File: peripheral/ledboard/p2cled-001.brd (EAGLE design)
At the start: 91 x 55 mm, 5 parts, among them J3 DISP, J4 PWR

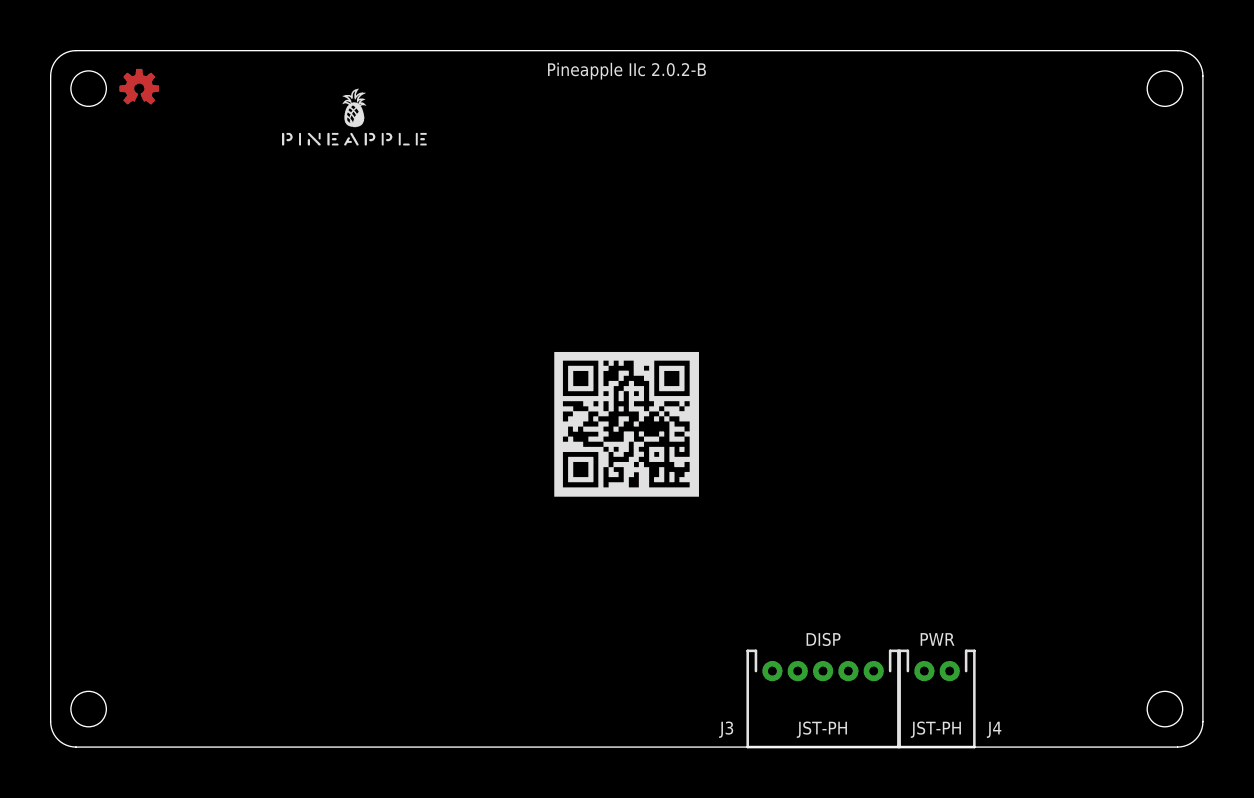
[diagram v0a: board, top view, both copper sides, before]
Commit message: Added LED board design.
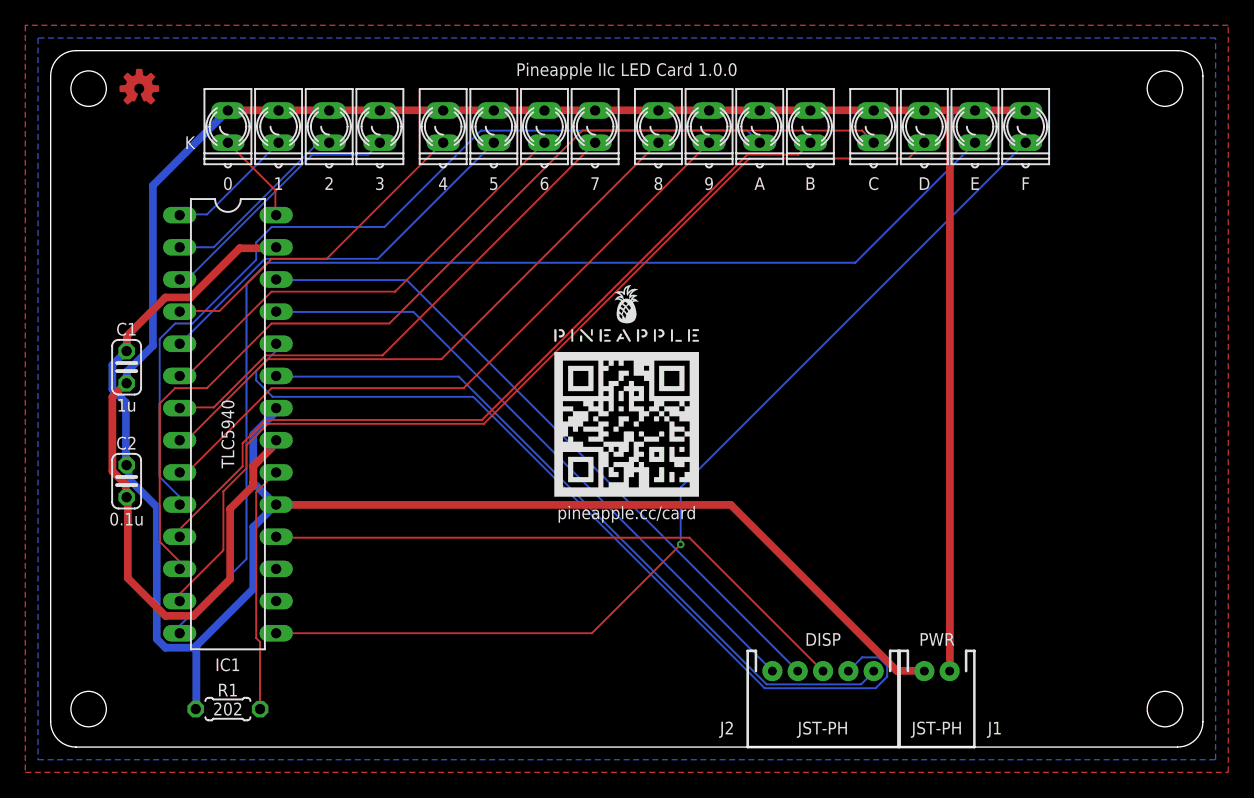
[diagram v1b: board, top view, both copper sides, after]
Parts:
- added 0, 1, 2, 3, 4, 5, 6, 7, 8, 9, A, B, C, D, E, F: (no value), led:Q62902-B152
- added C1: 1u, resistor:C025-024X044
- added C2: 0.1u, resistor:C025-024X044
- added IC1: TLC5940NT, tlc5940:DIL28-3
- added R1: 2k, resistor:0204/5
- moved U$1 26.5 mm to (45.5, 32.0)
- renumbered J3 to J2, J4 to J1
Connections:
- new net D5: IC1.23, J2.1
- new net D7: IC1.24, J2.2
- new net D8: IC1.18, J2.3
- new net MOSI: IC1.26, J2.4
- new net N$1: 0.K, IC1.28
- new net N$10: 9.K, IC1.9
- new net N$11: A.K, IC1.10
- new net N$12: B.K, IC1.11
- new net N$13: C.K, IC1.12
- new net N$14: D.K, IC1.13
- new net N$15: E.K, IC1.14
- new net N$16: F.K, IC1.15
- new net N$17: IC1.20, R1.2
- new net N$2: 1.K, IC1.1
- new net N$3: 2.K, IC1.2
- new net N$4: 3.K, IC1.3
- new net N$5: 4.K, IC1.4
- new net N$6: 5.K, IC1.5
- new net N$7: 6.K, IC1.6
- new net N$8: 7.K, IC1.7
- new net N$9: 8.K, IC1.8
- new net SCLK: IC1.25, J2.5
- net GND: now also C1.2, C2.2, IC1.19, IC1.22, IC1.27, R1.1
- net VCC: now also 0.A, 1.A, 2.A, 3.A, 4.A, 5.A, 6.A, 7.A, 8.A, 9.A, A.A, B.A, C.A, C1.1, C2.1, D.A, E.A, F.A, IC1.21
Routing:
- net VCC: track 0.00 -> 171.7 mm
- net GND: track 0.00 -> 128.5 mm
- net N$15: track 0.00 -> 92.0 mm
- net N$13: track 0.00 -> 79.5 mm
- net N$14: track 0.00 -> 77.9 mm
- net N$16: track 0.00 -> 77.9 mm, vias 0 -> 1
- net N$11: track 0.00 -> 69.1 mm
- net D7: track 0.00 -> 68.5 mm
- net N$12: track 0.00 -> 64.1 mm
- net D5: track 0.00 -> 57.8 mm
- net MOSI: track 0.00 -> 54.0 mm
- net N$10: track 0.00 -> 52.6 mm
- net SCLK: track 0.00 -> 51.0 mm
- net D8: track 0.00 -> 47.6 mm
- net N$9: track 0.00 -> 47.5 mm
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- added copper zone on layer 1, net GND
- added copper zone on layer 16, net GND
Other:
- board text added: "0.1u"
- board text added: "1u"
- board text added: "202"
- board text added: "K"
- board text added: "Pineapple IIc LED Card 1.0.0"
- board text added: "TLC5940"
- board text added: "pineapple.cc/card"
- board text removed: "Pineapple IIc 2.0.2-B"

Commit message: Fixed connection of LED board.
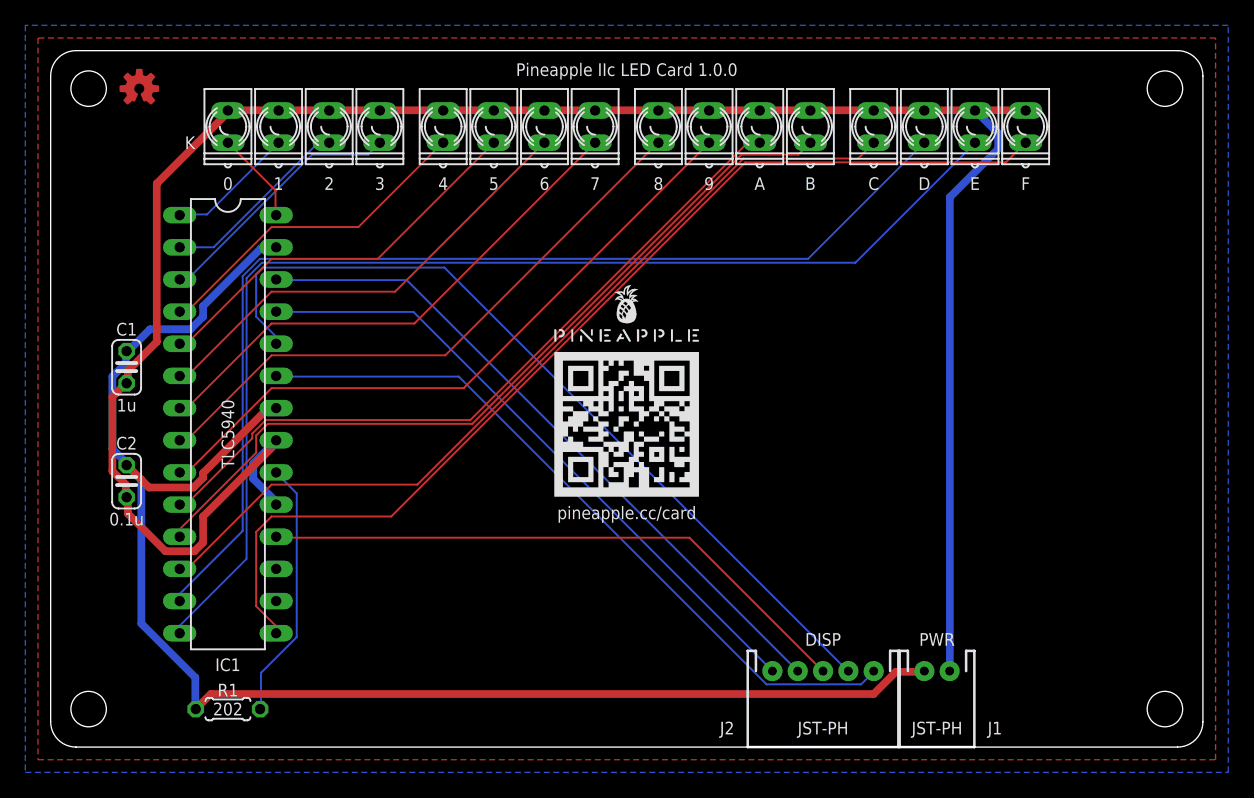
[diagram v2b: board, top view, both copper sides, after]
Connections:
- net GND: no longer IC1.19
- net VCC: now also IC1.19
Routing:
- net N$11: track 69.1 -> 57.9 mm
- net N$13: track 79.5 -> 68.8 mm
- net N$14: track 77.9 -> 85.9 mm
- net GND: track 128.5 -> 121.3 mm
- net N$16: track 77.9 -> 82.2 mm, vias 1 -> 0
- net D7: track 68.5 -> 66.4 mm
- net VCC: track 171.7 -> 170.4 mm
- net N$17: track 19.5 -> 20.6 mm
